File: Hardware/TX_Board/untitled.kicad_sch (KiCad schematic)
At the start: 50 parts, among them IC7 MAPS-010164-TR0500, IC8 QPA9122TR7, J13 MM8030-2610RJ3, J14 MM8030-2610RJ3, J15 Conn_Coaxial

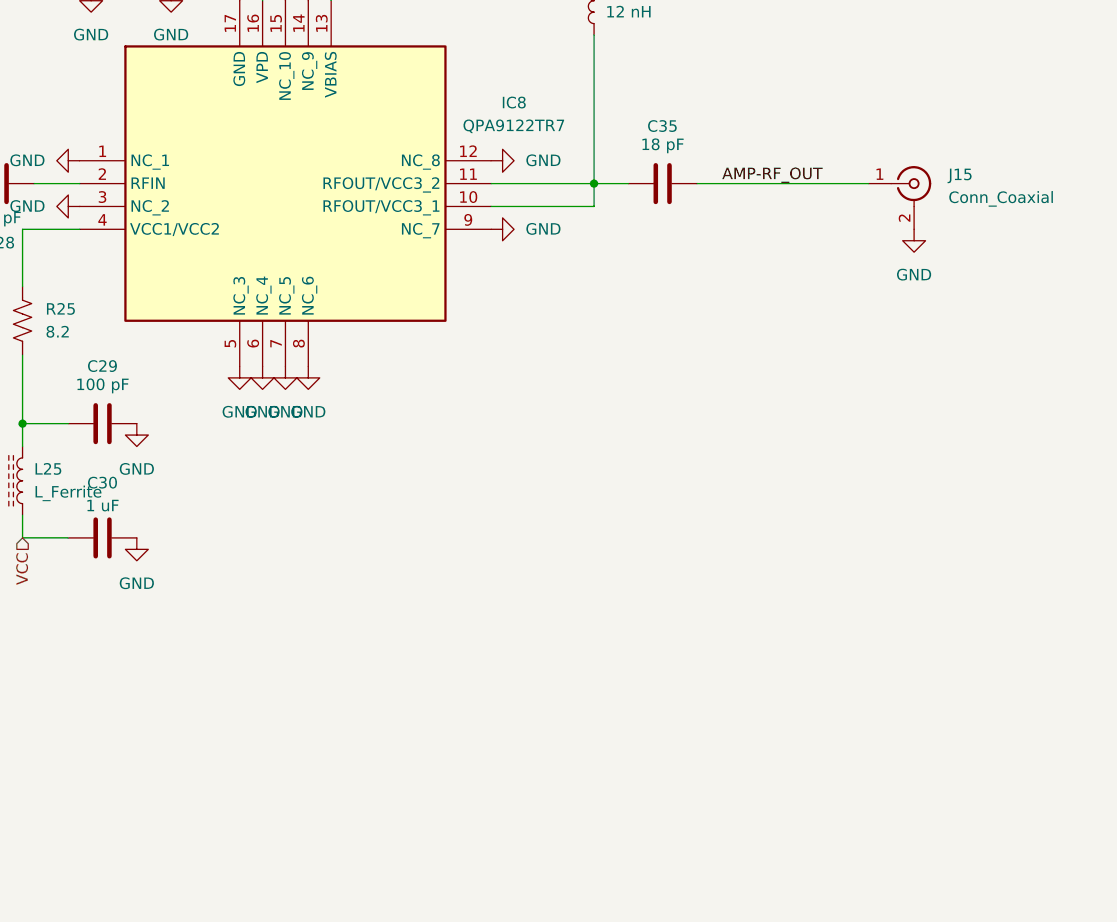
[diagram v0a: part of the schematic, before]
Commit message: RF test points, voltage test pads
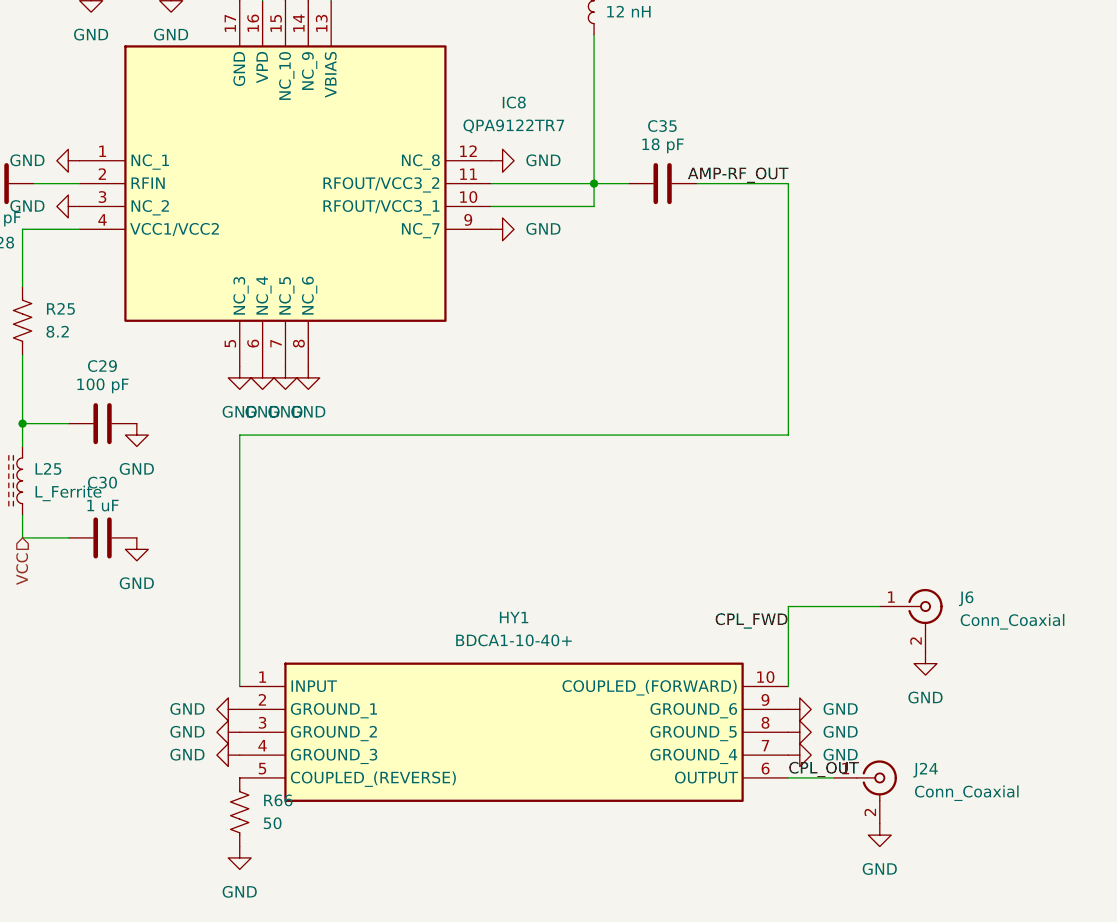
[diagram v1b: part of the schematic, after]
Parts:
- removed J15: Conn_Coaxial, Connector_Coaxial:SMA_Amphenol_132289_EdgeMount, symbol tx_board_symbol_library:Conn_Coaxial
- added HY1: BDCA1-10-40+, BDCA1-10-40+:BDCA11040, symbol BDCA1-10-40+:BDCA1-10-40+
- added J24: Conn_Coaxial, CONSMA001_SMD_G_T:LINX_CONSMA001-SMD-G-T, symbol tx_board_symbol_library:Conn_Coaxial
- added J6: Conn_Coaxial, Connector_Coaxial:SMA_Amphenol_132289_EdgeMount, symbol tx_board_symbol_library:Conn_Coaxial
- added R66: 50, Resistor_SMD:R_0402_1005Metric, symbol tx_board_symbol_library:R_US
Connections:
- net AMP-RF_OUT: now also HY1.1 (INPUT)
- net GND: now also HY1.2 (GROUND_1), HY1.3 (GROUND_2), HY1.4 (GROUND_3), HY1.7 (GROUND_4), HY1.8 (GROUND_5), HY1.9 (GROUND_6), J24.2 (Ext), J6.2 (Ext), R66.2
- new net: HY1.5 (COUPLED_(REVERSE)), R66.1
- new net CPL_FWD: HY1.10 (COUPLED_(FORWARD)), J6.1 (In)
- new net CPL_OUT: HY1.6 (OUTPUT), J24.1 (In)

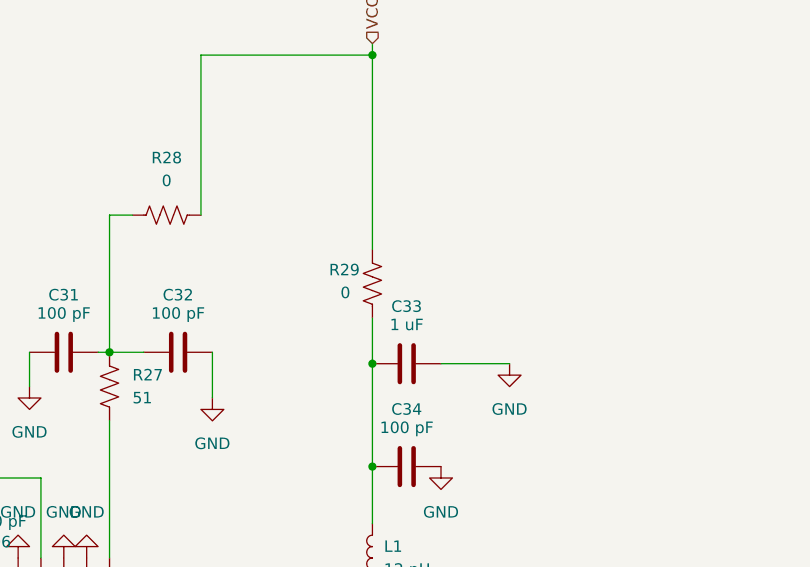
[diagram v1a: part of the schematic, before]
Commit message: resistor to ferrite
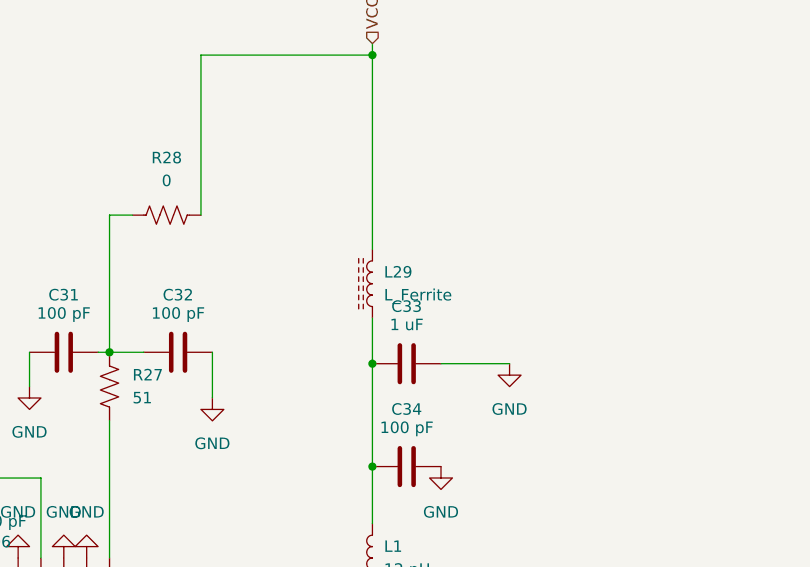
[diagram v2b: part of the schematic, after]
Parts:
- removed R29: 0, Resistor_SMD:R_0603_1608Metric, symbol tx_board_symbol_library:R_US
- added L29: L_Ferrite, Inductor_SMD:L_0201_0603Metric, symbol Device:L_Ferrite
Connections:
- net VCC: now also L29.2
- net at C33.1, C34.1, L1.2: now also L29.1
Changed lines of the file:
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@@
 	)
 	(symbol
-		(lib_id "tx_board_symbol_library:R_US")
-		(at 364.49 100.33 180)
-		(unit 1)
-		(exclude_from_sim no)
-		(in_bom yes)
-		(on_board yes)
-		(dnp no)
-		(property "Reference" "R29"
-			(at 359.664 98.806 0)
-			(effects
-				(font
-					(size 1.27 1.27)
-				)
-				(justify right)
-			)
-		)
-		(property "Value" "0"
-			(at 360.934 101.346 0)
-			(effects
-				(font
-					(size 1.27 1.27)
-				)
-				(justify right)
-			)
-		)
-		(property "Footprint" "Resistor_SMD:R_0603_1608Metric"
-			(at 363.474 100.076 90)
-			(effects
-				(font
-					(size 1.27 1.27)
-				)
-				(hide yes)
-			)
-		)
-		(property "Datasheet" "~"
-			(at 364.49 100.33 0)
-			(effects
-				(font
-					(size 1.27 1.27)
-				)
-				(hide yes)
-			)
-		)
-		(property "Description" "Resistor, US symbol"
-			(at 364.49 100.33 0)
-			(effects
-				(font
-					(size 1.27 1.27)
-				)
-				(hide yes)
-			)
-		)
-		(pin "1"
-		)
-		(pin "2"
-		)
-		(instances
-			(project "TX_Board"
-				(path "/ca6f0547-784a-45aa-9c4a-84ccc33d2bdf/20289cd5-7f64-400a-85b5-527b93622f25"
-					(reference "R41")
-					(unit 1)
-				)
-				(path "/ca6f0547-784a-45aa-9c4a-84ccc33d2bdf/29f67bc9-c244-44a6-89b9-0daa0a5c96e3"
-					(reference "R53")
-					(unit 1)
-				)
-				(path "/ca6f0547-784a-45aa-9c4a-84ccc33d2bdf/4e4b9e6c-a834-42ed-90e9-47de97e0b481"
-					(reference "R65")
-					(unit 1)
-				)
-				(path "/ca6f0547-784a-45aa-9c4a-84ccc33d2bdf/a3e338dc-9ba3-4797-a3b2-2c3d22ee34c6"
-					(reference "R29")
-					(unit 1)
-				)
-			)
-		)
-	)
-	(symbol
 		(lib_id "tx_board_symbol_library:GND")
 		(at 308.61 129.54 0)
@@
 					(unit 1)
 				)
+			)
+		)
+	)
+	(symbol
+		(lib_id "Device:L_Ferrite")
+		(at 364.49 100.33 180)
+		(unit 1)
+		(exclude_from_sim no)
+		(in_bom yes)
+		(on_board yes)
+		(dnp no)
+		(fields_autoplaced yes)
+		(property "Reference" "L29"
+			(at 365.76 99.0599 0)
+			(effects
+				(font
+					(size 1.27 1.27)
+				)
+				(justify right)
+			)
+		)
+		(property "Value" "L_Ferrite"
+			(at 365.76 101.5999 0)
+			(effects
+				(font
+					(size 1.27 1.27)
+				)
+				(justify right)
+			)
+		)
+		(property "Footprint" "Inductor_SMD:L_0201_0603Metric"
+			(at 364.49 100.33 0)
+			(effects
+				(font
+					(size 1.27 1.27)
+				)
+				(hide yes)
+			)
+		)
+		(property "Datasheet" "~"
+			(at 364.49 100.33 0)
+			(effects
+				(font
+					(size 1.27 1.27)
+				)
+				(hide yes)
+			)
+		)
+		(property "Description" "Inductor with ferrite core"
+			(at 364.49 100.33 0)
+			(effects
+				(font
+					(size 1.27 1.27)
+				)
+				(hide yes)
+			)
+		)
+		(pin "2"
+		)
+		(pin "1"
+		)
+		(instances
+			(project "TX_Board"
+				(path "/ca6f0547-784a-45aa-9c4a-84ccc33d2bdf/20289cd5-7f64-400a-85b5-527b93622f25"
+					(reference "L30")
+					(unit 1)
+				)
+				(path "/ca6f0547-784a-45aa-9c4a-84ccc33d2bdf/29f67bc9-c244-44a6-89b9-0daa0a5c96e3"
+					(reference "L31")
+					(unit 1)
+				)
+				(path "/ca6f0547-784a-45aa-9c4a-84ccc33d2bdf/4e4b9e6c-a834-42ed-90e9-47de97e0b481"
+					(reference "L32")
+					(unit 1)
+				)
+				(path "/ca6f0547-784a-45aa-9c4a-84ccc33d2bdf/a3e338dc-9ba3-4797-a3b2-2c3d22ee34c6"
+					(reference "L29")
+					(unit 1)
+				)
